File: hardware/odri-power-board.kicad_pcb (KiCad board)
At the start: 2 copper layers, 65 x 35 mm, 55 parts, among them IC1 LTC7001IMSE#PBF, J1 PROG, J10 OUT, J11 OUT, J12 OUT, J13 SW, J2 SPI, J3 IN, J4 OUT, J5 OUT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

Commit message: Harley's revision
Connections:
- net /5V renamed +5V
- net Net-(C10-Pad1) renamed /LOAD
- net Net-(C5-Pad1) renamed /GATE_CTRL
- net Net-(F1-Pad1) renamed +BATT
- C1 pad 1: /3V3 -> +3V3
- C17 pad 1: /3V3 -> +3V3
- C2 pad 1: /3V3 -> +3V3
- D1 pad 1: /3V3 -> +3V3
- D2 pad 1: /3V3 -> +3V3
- D2 pad 2: Net-(D2-Pad2) -> unconnected-(D2-DOUT-Pad2)
- IC1 pad 10: Net-(IC1-Pad10) -> unconnected-(IC1-NC-Pad10)
- J1 pad 1: /3V3 -> +3V3
- R1 pad 2: /3V3 -> +3V3
- U1 pad 1: /3V3 -> +3V3
- U1 pad 10: Net-(U1-Pad10) -> unconnected-(U1-PA0-Pad10)
- U1 pad 12: Net-(U1-Pad12) -> unconnected-(U1-PA2-Pad12)
- U1 pad 18: Net-(U1-Pad18) -> unconnected-(U1-PB0-Pad18)
- U1 pad 19: Net-(U1-Pad19) -> unconnected-(U1-PB1-Pad19)
- U1 pad 2: Net-(U1-Pad2) -> unconnected-(U1-PC13-Pad2)
- U1 pad 20: Net-(U1-Pad20) -> unconnected-(U1-PB2-Pad20)
- U1 pad 21: Net-(U1-Pad21) -> unconnected-(U1-PB10-Pad21)
- U1 pad 22: Net-(U1-Pad22) -> unconnected-(U1-PB11-Pad22)
- U1 pad 24: /3V3 -> unconnected-(U1-VDD-Pad24)
- U1 pad 29: Net-(U1-Pad29) -> unconnected-(U1-PA8-Pad29)
- U1 pad 3: Net-(U1-Pad3) -> unconnected-(U1-PC14-Pad3)
- U1 pad 30: Net-(U1-Pad30) -> unconnected-(U1-PA9-Pad30)
- U1 pad 31: Net-(U1-Pad31) -> unconnected-(U1-PA10-Pad31)
- U1 pad 32: Net-(U1-Pad32) -> unconnected-(U1-PA11-Pad32)
- U1 pad 33: Net-(U1-Pad33) -> unconnected-(U1-PA12-Pad33)
- U1 pad 34: /SWDIO -> unconnected-(U1-PA13-Pad34)
- U1 pad 36: /3V3 -> unconnected-(U1-VDD-Pad36)
- U1 pad 37: /SWCLK -> unconnected-(U1-PA14-Pad37)
- U1 pad 38: Net-(U1-Pad38) -> unconnected-(U1-PA15-Pad38)
- U1 pad 4: Net-(U1-Pad4) -> unconnected-(U1-PC15-Pad4)
- U1 pad 40: Net-(U1-Pad40) -> unconnected-(U1-PB4-Pad40)
- U1 pad 41: Net-(U1-Pad41) -> unconnected-(U1-PB5-Pad41)
- U1 pad 42: Net-(U1-Pad42) -> unconnected-(U1-PB6-Pad42)
- U1 pad 43: Net-(U1-Pad43) -> unconnected-(U1-PB7-Pad43)
- U1 pad 44: GND -> unconnected-(U1-BOOT0-Pad44)
- U1 pad 45: Net-(U1-Pad45) -> unconnected-(U1-PB8-Pad45)
- U1 pad 46: Net-(U1-Pad46) -> unconnected-(U1-PB9-Pad46)
- U1 pad 48: /3V3 -> unconnected-(U1-VDD-Pad48)
- U1 pad 5: Net-(U1-Pad5) -> unconnected-(U1-PD0-Pad5)
- U1 pad 6: Net-(U1-Pad6) -> unconnected-(U1-PD1-Pad6)
- U1 pad 7: /NRST -> unconnected-(U1-NRST-Pad7)
- U1 pad 9: /3V3 -> unconnected-(U1-VDDA-Pad9)
- U2 pad 3: Net-(U2-Pad3) -> unconnected-(U2-ALERT-Pad3)
- U3 pad 7: Net-(U3-Pad7) -> unconnected-(U3-NC-Pad7)
- U3 pad 8: Net-(U3-Pad8) -> unconnected-(U3-~{RESET}-Pad8)
- U4 pad 2: /3V3 -> +3V3
- X1 pad 1: /3V3 -> +3V3
- X1 pad 3: Net-(U1-Pad5) -> unconnected-(X1-OUT-Pad3)
- X1 pad 4: /3V3 -> +3V3
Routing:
- net (no net): track 0.00 -> 79.2 mm
- net /3V3: track 73.6 -> 0.00 mm
- net Net-(U1-Pad5): track 5.61 -> 0.00 mm
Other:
- net class Default removed
- net class HC removed
- net class HV removed

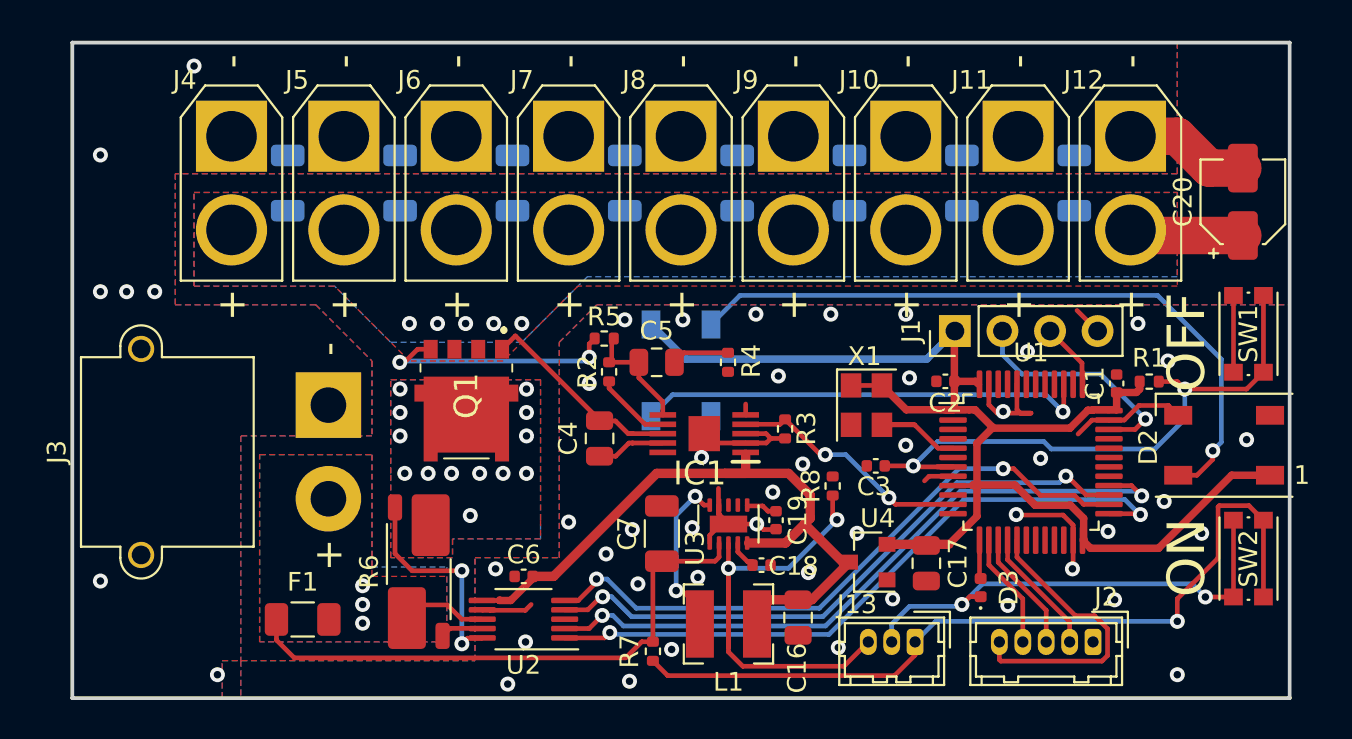
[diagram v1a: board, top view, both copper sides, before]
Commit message: add mounting holes and silkscreen
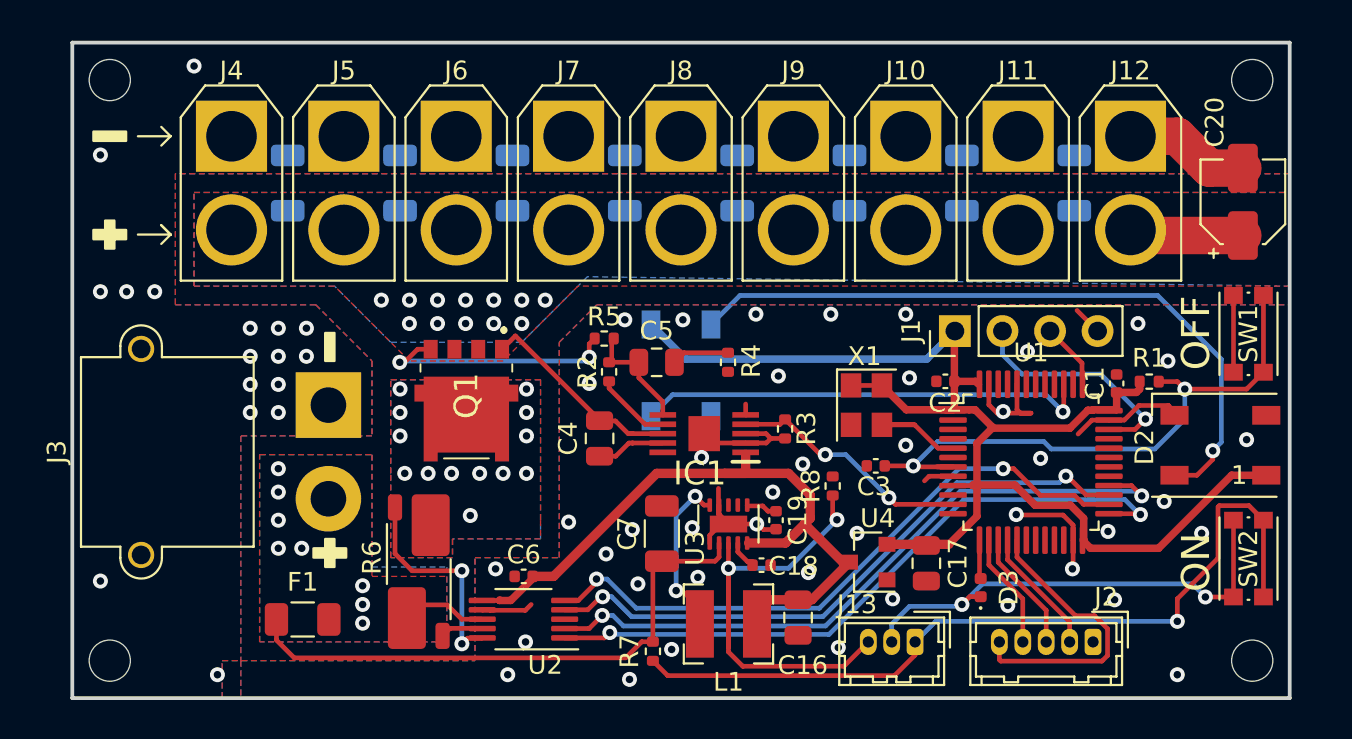
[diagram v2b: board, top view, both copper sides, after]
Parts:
- added G***: LOGO, LOGO, B.Cu at (54.0, 64.8)
- added REF**: MountingHole_2.2mm_M2_DIN965, MountingHole:MountingHole_2.2mm_M2_DIN965, F.Cu at (47.0, 68.0)
- added REF**: MountingHole_2.2mm_M2_DIN965, MountingHole:MountingHole_2.2mm_M2_DIN965, F.Cu at (108.0, 68.0)
- added REF**: MountingHole_2.2mm_M2_DIN965, MountingHole:MountingHole_2.2mm_M2_DIN965, F.Cu at (47.0, 37.0)
- added REF**: MountingHole_2.2mm_M2_DIN965, MountingHole:MountingHole_2.2mm_M2_DIN965, F.Cu at (108.0, 37.0)
- moved D2 0.20 mm to (106.3, 56.5)
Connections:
- U1 pad 24: unconnected-(U1-VDD-Pad24) -> +3V3
- U1 pad 34: unconnected-(U1-PA13-Pad34) -> /SWDIO
- U1 pad 36: unconnected-(U1-VDD-Pad36) -> +3V3
- U1 pad 37: unconnected-(U1-PA14-Pad37) -> /SWCLK
- U1 pad 44: unconnected-(U1-BOOT0-Pad44) -> GND
- U1 pad 48: unconnected-(U1-VDD-Pad48) -> +3V3
- U1 pad 5: unconnected-(U1-PD0-Pad5) -> /CLK_SGN
- U1 pad 7: unconnected-(U1-NRST-Pad7) -> /NRST
- U1 pad 9: unconnected-(U1-VDDA-Pad9) -> +3V3
- X1 pad 3: unconnected-(X1-OUT-Pad3) -> /CLK_SGN
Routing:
- net (no net): track 79.2 -> 0.00 mm
- net +3V3: track 0.00 -> 73.6 mm
- net /CLK_SGN: track 0.00 -> 5.61 mm
- net GND: vias 49 -> 59
- net /LOAD: vias 5 -> 12
- net +BATT: vias 3 -> 8
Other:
- board text added: "LAAS - CNRS - A2S"
- board text added: "O.D.R.I. Power Board V1R1"
- board text added: "github.com/a2s-institute/power-board"
- board text removed: "LAAS - CNRS"
- board text removed: "O.D.R.I. Power Board V1"
- board text removed: "github.com/open-dynamic-robot-initiative/power-board"
